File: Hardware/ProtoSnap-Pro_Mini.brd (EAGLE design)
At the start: 39.4 x 63.5 mm, 66 parts, among them Q1 16MHz, U1 ATMEGA328, U2 MIC5205, U3 FT232RLSSOP, U4 TEMT6000, X2 USB-SMD-NS

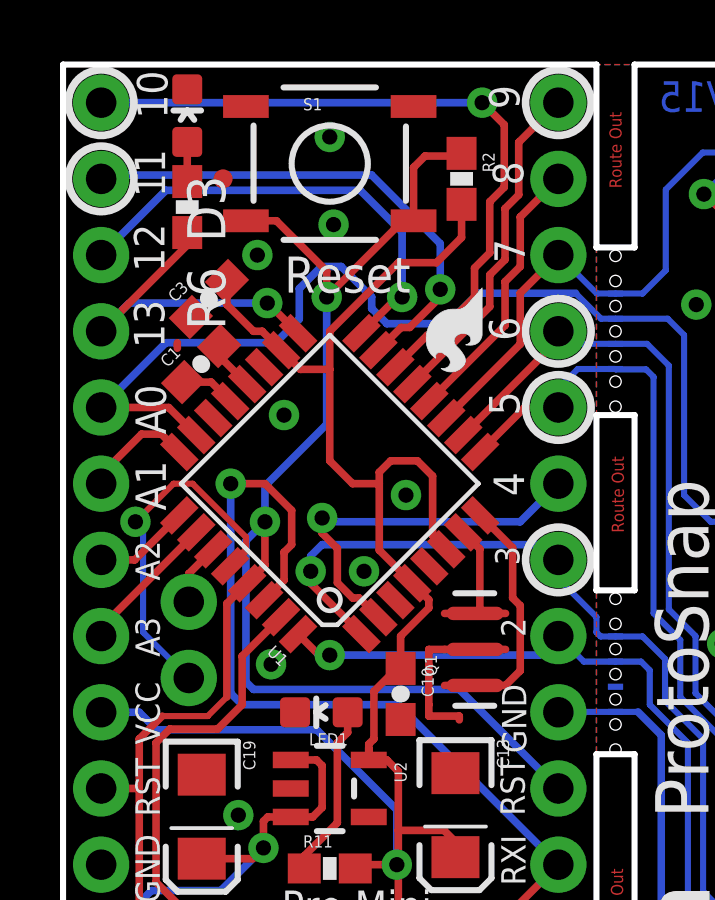
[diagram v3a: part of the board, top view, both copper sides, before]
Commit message: Switched to flags in sch, added new frame
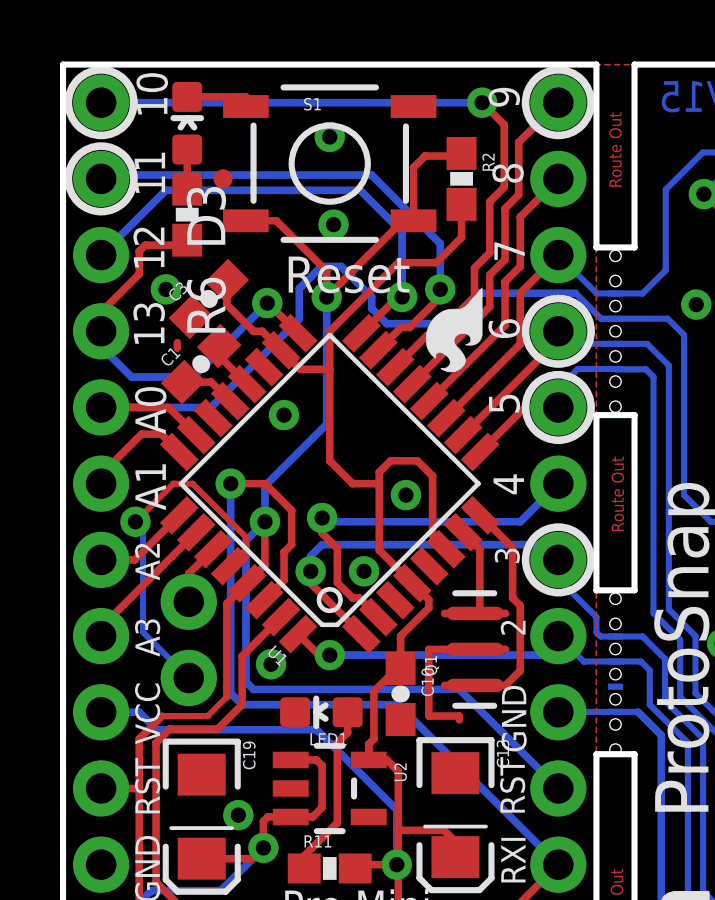
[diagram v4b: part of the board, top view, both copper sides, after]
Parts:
- added FRAME1: FRAME-LETTER, SparkFun-Aesthetics:CREATIVE_COMMONS
- moved D3 0.25 mm to (4.14, 61.5)
- moved R6 0.25 mm to (4.14, 58.5)
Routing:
- net GND: track 82.2 -> 84.5 mm
- net SCK: track 11.8 -> 14.0 mm
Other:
- board text added: "Jim Lindblom"
- board text added: "Revised by Pete Lewis"
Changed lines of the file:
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@@
 <layer number="27" name="tValues" color="7" fill="1" visible="no" active="yes"/>
 <layer number="28" name="bValues" color="7" fill="1" visible="no" active="yes"/>
-<layer number="29" name="tStop" color="7" fill="3" visible="yes" active="yes"/>
+<layer number="29" name="tStop" color="7" fill="3" visible="no" active="yes"/>
 <layer number="30" name="bStop" color="7" fill="6" visible="no" active="yes"/>
 <layer number="31" name="tCream" color="7" fill="4" visible="no" active="yes"/>
@@
 <layer number="106" name="bPlate" color="7" fill="1" visible="no" active="yes"/>
 <layer number="107" name="Crop" color="7" fill="1" visible="no" active="yes"/>
-<layer number="108" name="tplace-old" color="10" fill="1" visible="yes" active="yes"/>
-<layer number="109" name="ref-old" color="11" fill="1" visible="yes" active="yes"/>
+<layer number="108" name="tplace-old" color="10" fill="1" visible="no" active="yes"/>
+<layer number="109" name="ref-old" color="11" fill="1" visible="no" active="yes"/>
 <layer number="116" name="Patch_BOT" color="9" fill="4" visible="no" active="yes"/>
 <layer number="121" name="_tsilk" color="7" fill="1" visible="no" active="yes"/>
@@
 <layer number="144" name="Drill_legend" color="7" fill="1" visible="no" active="yes"/>
 <layer number="151" name="HeatSink" color="7" fill="1" visible="no" active="yes"/>
-<layer number="199" name="Contour" color="7" fill="1" visible="yes" active="yes"/>
+<layer number="199" name="Contour" color="7" fill="1" visible="no" active="yes"/>
 <layer number="200" name="200bmp" color="1" fill="10" visible="no" active="no"/>
 <layer number="201" name="201bmp" color="2" fill="1" visible="no" active="no"/>
@@
 <text x="18.2118" y="61.9252" size="0.4064" layer="1" font="vector" ratio="15" rot="R270">Route Out</text>
 <text x="22.3012" y="61.9252" size="1.016" layer="16" font="vector" ratio="15" rot="MR0">V15</text>
+<text x="19.05" y="-10.16" size="1.778" layer="51" font="vector" ratio="10">Jim Lindblom</text>
+<text x="19.05" y="-12.7" size="1.778" layer="51" font="vector" ratio="10">Revised by Pete Lewis</text>
 </plain>
 <attributes>
@@
 <attribute name="VALUE" x="4.757503125" y="52.268265625" size="0.4064" layer="27" rot="R45"/>
 </element>
-<element name="R6" library="SparkFun" package="0603-RES" value="330" x="4.1402" y="58.7502" smashed="yes" rot="R90">
-<attribute name="NAME" x="4.1402" y="56.7502" size="1.27" layer="25" rot="R270"/>
-<attribute name="VALUE" x="4.7752" y="59.0926" size="0.4064" layer="27" rot="R270"/>
-</element>
-<element name="D3" library="Testing" package="0603-LED-ALT1" value="Green" x="4.1402" y="61.7982" smashed="yes">
-<attribute name="NAME" x="4.1402" y="59.7982" size="1.27" layer="25" rot="R270"/>
-<attribute name="VALUE" x="4.8006" y="62.547" size="0.4064" layer="27" rot="R270"/>
+<element name="R6" library="SparkFun" package="0603-RES" value="330" x="4.1402" y="58.4962" smashed="yes" rot="R90">
+<attribute name="NAME" x="4.1402" y="56.4962" size="1.27" layer="25" rot="R270"/>
+<attribute name="VALUE" x="4.7752" y="58.8386" size="0.4064" layer="27" rot="R270"/>
+</element>
+<element name="D3" library="Testing" package="0603-LED-ALT1" value="Green" x="4.1402" y="61.5442" smashed="yes">
+<attribute name="NAME" x="4.1402" y="59.5442" size="1.27" layer="25" rot="R270"/>
+<attribute name="VALUE" x="4.8006" y="62.293" size="0.4064" layer="27" rot="R270"/>
 </element>
 <element name="U$11" library="SparkFun" package="SFE-NEW-WEBLOGO" value="LOGO-SFENEW" x="8.763" y="36.322" rot="MR90"/>
@@
 <element name="S1" library="Testing" package="TACTILE-SWITCH-SMD-ALT01" value="" x="8.89" y="60.198"/>
 <element name="S2" library="Testing" package="TACTILE-SWITCH-SMD-ALT01" value="" x="34.036" y="59.69"/>
+<element name="FRAME1" library="SparkFun-Aesthetics" package="CREATIVE_COMMONS" value="FRAME-LETTER" x="-11.96045625" y="-10.16"/>
 </elements>
 <signals>
@@
 <contactref element="S1" pad="1"/>
 <contactref element="S1" pad="2"/>
-<via x="6.477" y="57.15" extent="1-16" drill="0.508"/>
+<via x="3.429" y="56.007" extent="1-16" drill="0.508"/>
 <via x="9.017" y="58.166" extent="1-16" drill="0.508"/>
 <contactref element="S2" pad="3"/>
@@
 <wire x1="12.192" y1="41.783" x2="13.208" y2="41.783" width="0.254" layer="1"/>
 <wire x1="13.208" y1="41.783" x2="13.208" y2="41.656" width="0.254" layer="1"/>
-<wire x1="12.192" y1="43.478640625" x2="12.192" y2="42.164" width="0.254" layer="1"/>
-<wire x1="12.192" y1="42.164" x2="12.192" y2="41.783" width="0.254" layer="1"/>
+<wire x1="12.192" y1="44.0046" x2="12.192" y2="41.783" width="0.254" layer="1"/>
 <wire x1="12.717959375" y1="44.0046" x2="12.192" y2="44.0046" width="0.254" layer="1"/>
-<wire x1="12.192" y1="44.0046" x2="12.192" y2="43.478640625" width="0.254" layer="1"/>
-<wire x1="6.477" y1="57.15" x2="4.260875" y2="55.086275" width="0" layer="19" extent="1-1"/>
+<wire x1="4.1402" y1="62.4212" x2="6.096" y2="62.4212" width="0.254" layer="1"/>
+<wire x1="6.096" y1="62.4212" x2="6.096" y2="62.103" width="0.254" layer="1"/>
 </signal>
 <signal name="AREF">
@@
 <contactref element="JP6" pad="9"/>
 <contactref element="U1" pad="17"/>
-<wire x1="1.27" y1="54.61" x2="4.1402" y2="57.4802" width="0.254" layer="1"/>
 <wire x1="7.834571875" y1="54.545225" x2="6.829996875" y2="55.5498" width="0.254" layer="1"/>
 <wire x1="6.829996875" y1="55.5498" x2="6.8072" y2="55.5498" width="0.254" layer="1"/>
 <via x="6.8072" y="55.5498" extent="1-16" drill="0.508"/>
-<wire x1="6.8072" y1="55.5498" x2="2.2098" y2="55.5498" width="0.254" layer="16"/>
-<wire x1="2.2098" y1="55.5498" x2="1.27" y2="54.61" width="0.254" layer="16"/>
-<wire x1="4.1402" y1="57.4802" x2="4.1402" y2="57.9002" width="0.254" layer="1"/>
+<wire x1="4.1402" y1="57.4802" x2="4.1402" y2="57.6462" width="0.254" layer="1"/>
+<wire x1="6.8072" y1="55.5498" x2="4.3434" y2="53.086" width="0.254" layer="16"/>
+<wire x1="4.3434" y1="53.086" x2="2.286" y2="53.086" width="0.254" layer="16"/>
+<wire x1="2.286" y1="53.086" x2="1.27" y2="54.102" width="0.254" layer="16"/>
+<wire x1="1.27" y1="54.102" x2="1.27" y2="54.61" width="0.254" layer="16"/>
+<wire x1="4.1402" y1="57.4802" x2="2.7432" y2="57.4802" width="0.254" layer="1"/>
+<wire x1="2.7432" y1="57.4802" x2="2.54" y2="57.277" width="0.254" layer="1"/>
+<wire x1="2.54" y1="57.277" x2="2.54" y2="56.515" width="0.254" layer="1"/>
+<wire x1="2.54" y1="56.515" x2="1.27" y2="55.245" width="0.254" layer="1"/>
+<wire x1="1.27" y1="55.245" x2="1.27" y2="54.61" width="0.254" layer="1"/>
 </signal>
 <signal name="N$38">
@@
 <contactref element="R6" pad="2"/>
 <contactref element="D3" pad="A"/>
-<wire x1="4.1402" y1="60.9212" x2="4.1402" y2="59.6002" width="0.254" layer="1"/>
+<wire x1="4.1402" y1="60.6672" x2="4.1402" y2="59.3462" width="0.254" layer="1"/>
 </signal>
 <signal name="RAW" class="1">
@@
 <wire x1="32.4" y1="48.91" x2="33.87" y2="50.38" width="0.254" layer="1"/>
 <wire x1="33.87" y1="50.38" x2="33.87" y2="50.8" width="0.254" layer="1"/>
-<wire x1="7.874" y1="55.0164" x2="7.0866" y2="54.229" width="0.254" layer="16"/>
-<wire x1="7.0866" y1="54.229" x2="3.429" y2="54.229" width="0.254" layer="16"/>
-<wire x1="3.429" y1="54.229" x2="1.27" y2="52.07" width="0.254" layer="16"/>
 <wire x1="4.440459375" y1="51.1511125" x2="3.521571875" y2="52.07" width="0.254" layer="1"/>
 <wire x1="3.521571875" y1="52.07" x2="1.27" y2="52.07" width="0.254" layer="1"/>
@@
 <wire x1="10.287" y1="55.372" x2="10.287" y2="55.753" width="0.254" layer="16"/>
 <wire x1="10.287" y1="55.753" x2="9.271" y2="56.769" width="0.254" layer="16"/>
+<wire x1="7.874" y1="55.0164" x2="4.9276" y2="52.07" width="0.254" layer="16"/>
+<wire x1="4.9276" y1="52.07" x2="1.27" y2="52.07" width="0.254" layer="16"/>
 </signal>
 <signal name="D2">

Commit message: added OSHW logo
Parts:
- added LOGO1: OSHW-LOGOS, SparkFun-Aesthetics:OSHW-LOGO-S
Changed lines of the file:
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@@
 <element name="S2" library="Testing" package="TACTILE-SWITCH-SMD-ALT01" value="" x="34.036" y="59.69"/>
 <element name="FRAME1" library="SparkFun-Aesthetics" package="CREATIVE_COMMONS" value="FRAME-LETTER" x="-11.96045625" y="-10.16"/>
+<element name="LOGO1" library="SparkFun-Aesthetics" package="OSHW-LOGO-S" value="OSHW-LOGOS" x="21.082" y="61.468" rot="R90"/>
 </elements>
 <signals>

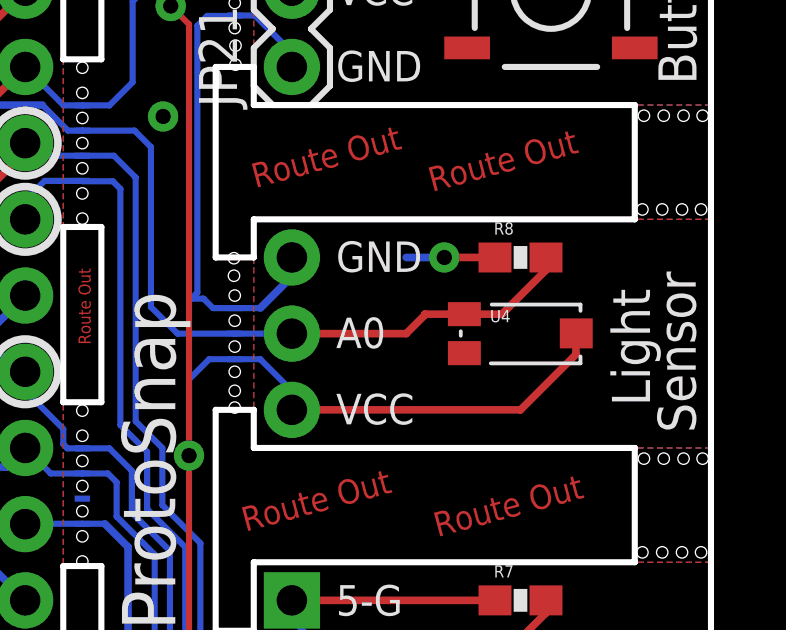
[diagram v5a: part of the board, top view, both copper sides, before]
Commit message: Switched light sensor to ALS-PT19
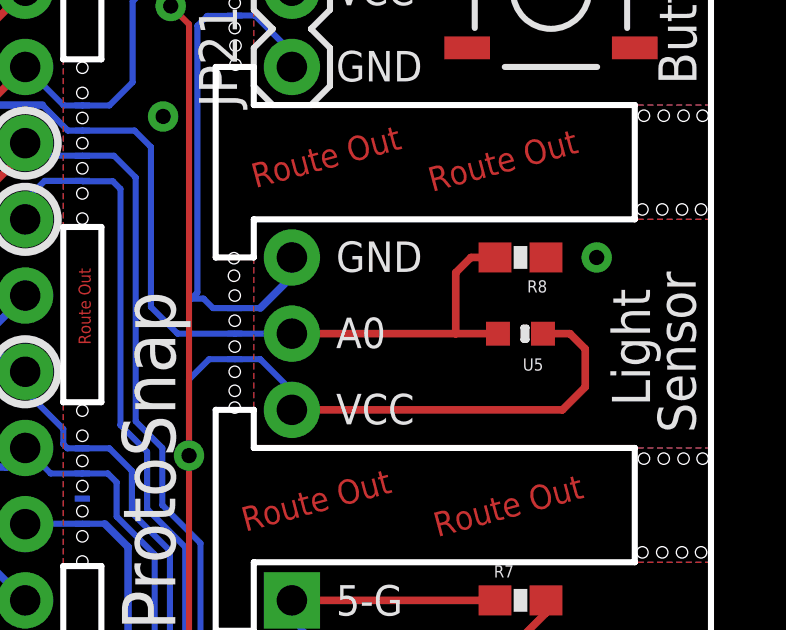
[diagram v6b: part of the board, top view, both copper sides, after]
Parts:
- removed U4: TEMT6000, SparkFun:TEMT6000-SEN
- added U5: ALS-PT19, SparkFun-Sensors:ALS-PT19
- turned R8 to 180 degrees
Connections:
- net A0: now also U5.E; no longer U4.EMITTER
- net VCC: now also U5.C; no longer U4.COLLECTOR
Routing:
- net GND: track 84.5 -> 81.5 mm
- net VCC: track 184.6 -> 186.6 mm
- net A0: track 47.7 -> 48.4 mm
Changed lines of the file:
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@@
 <setting verticaltext="up"/>
 </settings>
-<grid distance="0.05" unitdist="inch" unit="inch" style="lines" multiple="1" display="yes" altdistance="0.005" altunitdist="inch" altunit="inch"/>
+<grid distance="0.05" unitdist="inch" unit="inch" style="lines" multiple="1" display="yes" altdistance="0.025" altunitdist="inch" altunit="inch"/>
 <layers>
 <layer number="1" name="Top" color="4" fill="1" visible="yes" active="yes"/>
@@
 <element name="R7" library="SparkFun" package="0603-RES" value="100" x="33.02" y="39.37"/>
 <element name="SG1" library="SparkFun" package="BUZZER-CCV" value="BUZZERSMD2" x="31.75" y="20.32" rot="R90"/>
-<element name="U4" library="SparkFun" package="TEMT6000-SEN" value="TEMT6000" x="33.02" y="48.26"/>
-<element name="R8" library="SparkFun" package="0603-RES" value="10k" x="33.02" y="50.8"/>
+<element name="R8" library="SparkFun" package="0603-RES" value="10k" x="33.02" y="50.8" rot="R180"/>
 <element name="JP8" library="SparkFun" package="1X04" value="" x="25.4" y="39.37" rot="MR270"/>
 <element name="JP9" library="SparkFun" package="1X02" value="" x="25.4" y="19.05" rot="MR90"/>
@@
 <element name="FRAME1" library="SparkFun-Aesthetics" package="CREATIVE_COMMONS" value="FRAME-LETTER" x="-11.96045625" y="-10.16"/>
 <element name="LOGO1" library="SparkFun-Aesthetics" package="OSHW-LOGO-S" value="OSHW-LOGOS" x="21.082" y="61.468" rot="R90"/>
+<element name="U5" library="SparkFun-Sensors" package="ALS-PT19" value="ALS-PT19" x="33.02" y="48.26" rot="R180">
+<attribute name="PROD_ID" value="IC-11836" x="33.02" y="48.26" size="1.778" layer="27" font="vector" ratio="15" rot="R180" display="off"/>
+</element>
 </elements>
 <signals>
@@
 <wire x1="28.13" y1="16.32" x2="31.75" y2="16.32" width="0.254" layer="1"/>
 <wire x1="25.4" y1="19.05" x2="28.13" y2="16.32" width="0.254" layer="1"/>
-<wire x1="30.48" y1="50.8" x2="32.17" y2="50.8" width="0.254" layer="1"/>
-<wire x1="29.21" y1="50.8" x2="30.48" y2="50.8" width="0.254" layer="16"/>
 <wire x1="23.495" y1="49.1109" x2="24.3459" y2="49.1109" width="0.2032" layer="16"/>
 <wire x1="25.4" y1="50.165" x2="25.4" y2="50.8" width="0.254" layer="16"/>
@@
 <via x="1.2446" y="15.9766" extent="1-16" drill="0.508"/>
 <via x="10.668" y="28.575" extent="1-16" drill="0.508"/>
-<via x="30.48" y="50.8" extent="1-16" drill="0.508"/>
 <via x="19.939" y="33.147" extent="1-16" drill="0.508"/>
 <via x="21.1074" y="55.499" extent="1-16" drill="0.508"/>
@@
 <wire x1="4.1402" y1="62.4212" x2="6.096" y2="62.4212" width="0.254" layer="1"/>
 <wire x1="6.096" y1="62.4212" x2="6.096" y2="62.103" width="0.254" layer="1"/>
+<via x="35.56" y="50.8" extent="1-16" drill="0.508"/>
 </signal>
 <signal name="AREF">
@@
 <contactref element="JP6" pad="8"/>
 <contactref element="U1" pad="23"/>
-<contactref element="U4" pad="EMITTER"/>
 <contactref element="R8" pad="2"/>
 <contactref element="U$9" pad="P$2"/>
 <contactref element="JP10" pad="2"/>
 <contactref element="U$13" pad="P$3"/>
-<wire x1="29.83" y1="48.91" x2="31.15" y2="48.91" width="0.254" layer="1"/>
-<wire x1="29.83" y1="48.88" x2="29.83" y2="48.91" width="0.254" layer="1"/>
-<wire x1="29.21" y1="48.26" x2="29.83" y2="48.88" width="0.254" layer="1"/>
-<wire x1="25.4" y1="48.26" x2="29.21" y2="48.26" width="0.254" layer="1"/>
+<wire x1="25.4" y1="48.26" x2="30.861" y2="48.26" width="0.254" layer="1"/>
+<wire x1="30.861" y1="48.26" x2="32.27" y2="48.26" width="0.254" layer="1"/>
 <wire x1="23.495" y1="48.26" x2="25.4" y2="48.26" width="0.2032" layer="16"/>
 <wire x1="13.843" y1="55.88" x2="17.084" y2="55.88" width="0.254" layer="16"/>
@@
 <wire x1="20.701" y1="49.149" x2="21.59" y2="48.26" width="0.2032" layer="16"/>
 <wire x1="20.701" y1="54.483" x2="20.701" y2="49.149" width="0.2032" layer="16"/>
-<wire x1="31.15" y1="48.91" x2="32.4" y2="48.91" width="0.254" layer="1"/>
-<wire x1="32.4" y1="48.91" x2="33.87" y2="50.38" width="0.254" layer="1"/>
-<wire x1="33.87" y1="50.38" x2="33.87" y2="50.8" width="0.254" layer="1"/>
 <wire x1="4.440459375" y1="51.1511125" x2="3.521571875" y2="52.07" width="0.254" layer="1"/>
 <wire x1="3.521571875" y1="52.07" x2="1.27" y2="52.07" width="0.254" layer="1"/>
@@
 <wire x1="7.874" y1="55.0164" x2="4.9276" y2="52.07" width="0.254" layer="16"/>
 <wire x1="4.9276" y1="52.07" x2="1.27" y2="52.07" width="0.254" layer="16"/>
+<contactref element="U5" pad="E"/>
+<wire x1="32.17" y1="50.8" x2="31.369" y2="50.8" width="0.254" layer="1"/>
+<wire x1="31.369" y1="50.8" x2="30.861" y2="50.292" width="0.254" layer="1"/>
+<wire x1="30.861" y1="50.292" x2="30.861" y2="48.26" width="0.254" layer="1"/>
 </signal>
 <signal name="D2">
@@
 <contactref element="U3" pad="4"/>
 <contactref element="LED4" pad="A"/>
-<contactref element="U4" pad="COLLECTOR"/>
 <contactref element="JP8" pad="4"/>
 <contactref element="U$22" pad="P$4"/>
@@
 <wire x1="25.4" y1="31.75" x2="35.56" y2="31.75" width="0.254" layer="16"/>
 <wire x1="9.7155" y1="27.686" x2="9.7155" y2="29.845" width="0.2032" layer="16"/>
-<wire x1="34.87" y1="48.26" x2="34.88" y2="48.27" width="0.2032" layer="1"/>
-<wire x1="34.87" y1="47.57" x2="34.87" y2="48.26" width="0.254" layer="1"/>
-<wire x1="33.02" y1="45.72" x2="34.87" y2="47.57" width="0.254" layer="1"/>
-<wire x1="25.4" y1="45.72" x2="33.02" y2="45.72" width="0.254" layer="1"/>
 <wire x1="23.495" y1="47.4091" x2="24.3459" y2="47.4091" width="0.2032" layer="16"/>
 <wire x1="25.4" y1="46.355" x2="25.4" y2="45.72" width="0.2032" layer="16"/>
@@
 <wire x1="10.3632" y1="41.021" x2="10.1901" y2="40.8479" width="0.254" layer="1"/>
 <wire x1="10.1901" y1="40.8479" x2="10.1901" y2="40.32" width="0.254" layer="1"/>
+<contactref element="U5" pad="C"/>
+<wire x1="25.4" y1="45.72" x2="34.417" y2="45.72" width="0.254" layer="1"/>
+<wire x1="34.417" y1="45.72" x2="35.179" y2="46.482" width="0.254" layer="1"/>
+<wire x1="35.179" y1="46.482" x2="35.179" y2="47.752" width="0.254" layer="1"/>
+<wire x1="35.179" y1="47.752" x2="34.671" y2="48.26" width="0.254" layer="1"/>
+<wire x1="34.671" y1="48.26" x2="33.77" y2="48.26" width="0.254" layer="1"/>
 </signal>
 <signal name="N$5">

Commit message: changed micro fiducials to regular size
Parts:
- removed JP16, JP19, JP20, JP22: FIDUCIAL1X2.5, abes:FIDUCIAL-1X2.5
- added FID1, FID2: FIDUCIAL1X2, SparkFun-Aesthetics:FIDUCIAL-1X2
